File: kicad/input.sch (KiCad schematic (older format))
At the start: 4 parts, among them J2 EXTERNAL_OUT, J3 EXTERNAL_IN

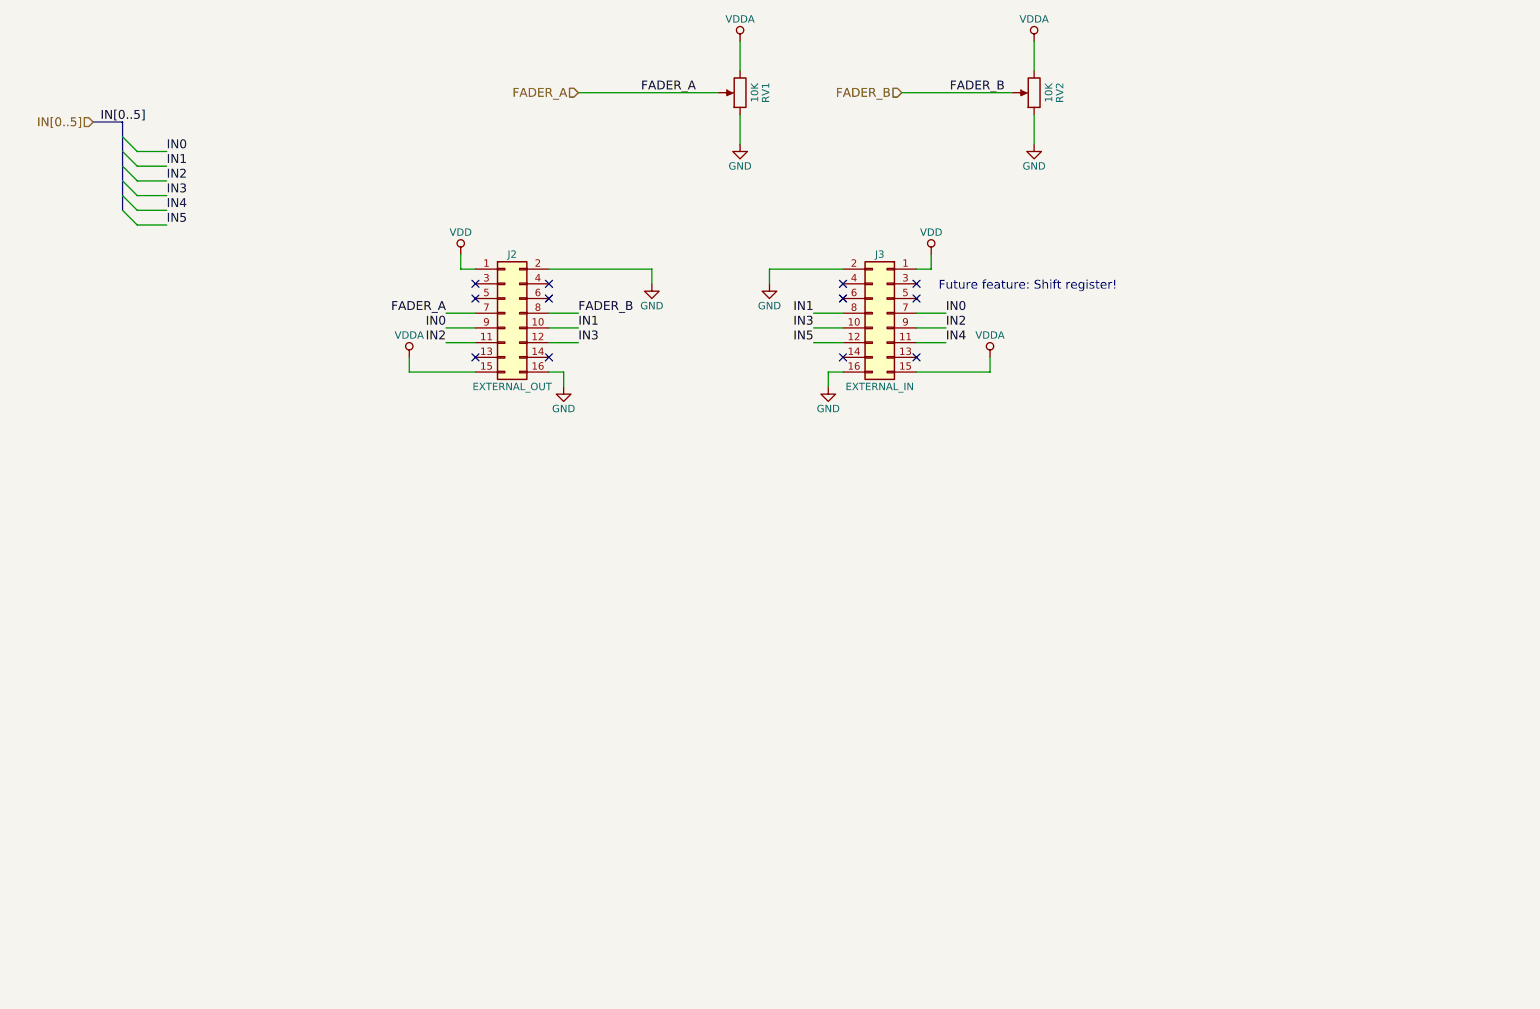
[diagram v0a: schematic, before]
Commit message: Created shift register circuitry and imported footprints
I think 5MHz to 10MHz is the theoretical maximum of this circuit. Actual
frequency will probably be around 5MHz or somewhat less given the signal
integrity issues on a 2-layer board with this many plane breaks.

Created footprints for button and HTSSOP

The HTSSOP footprint is special because I plan to hand solder, so I
added excessive thermal vias and a bare pad on the backside.

The netlist is imported to the PCB, but only the switches are placed.
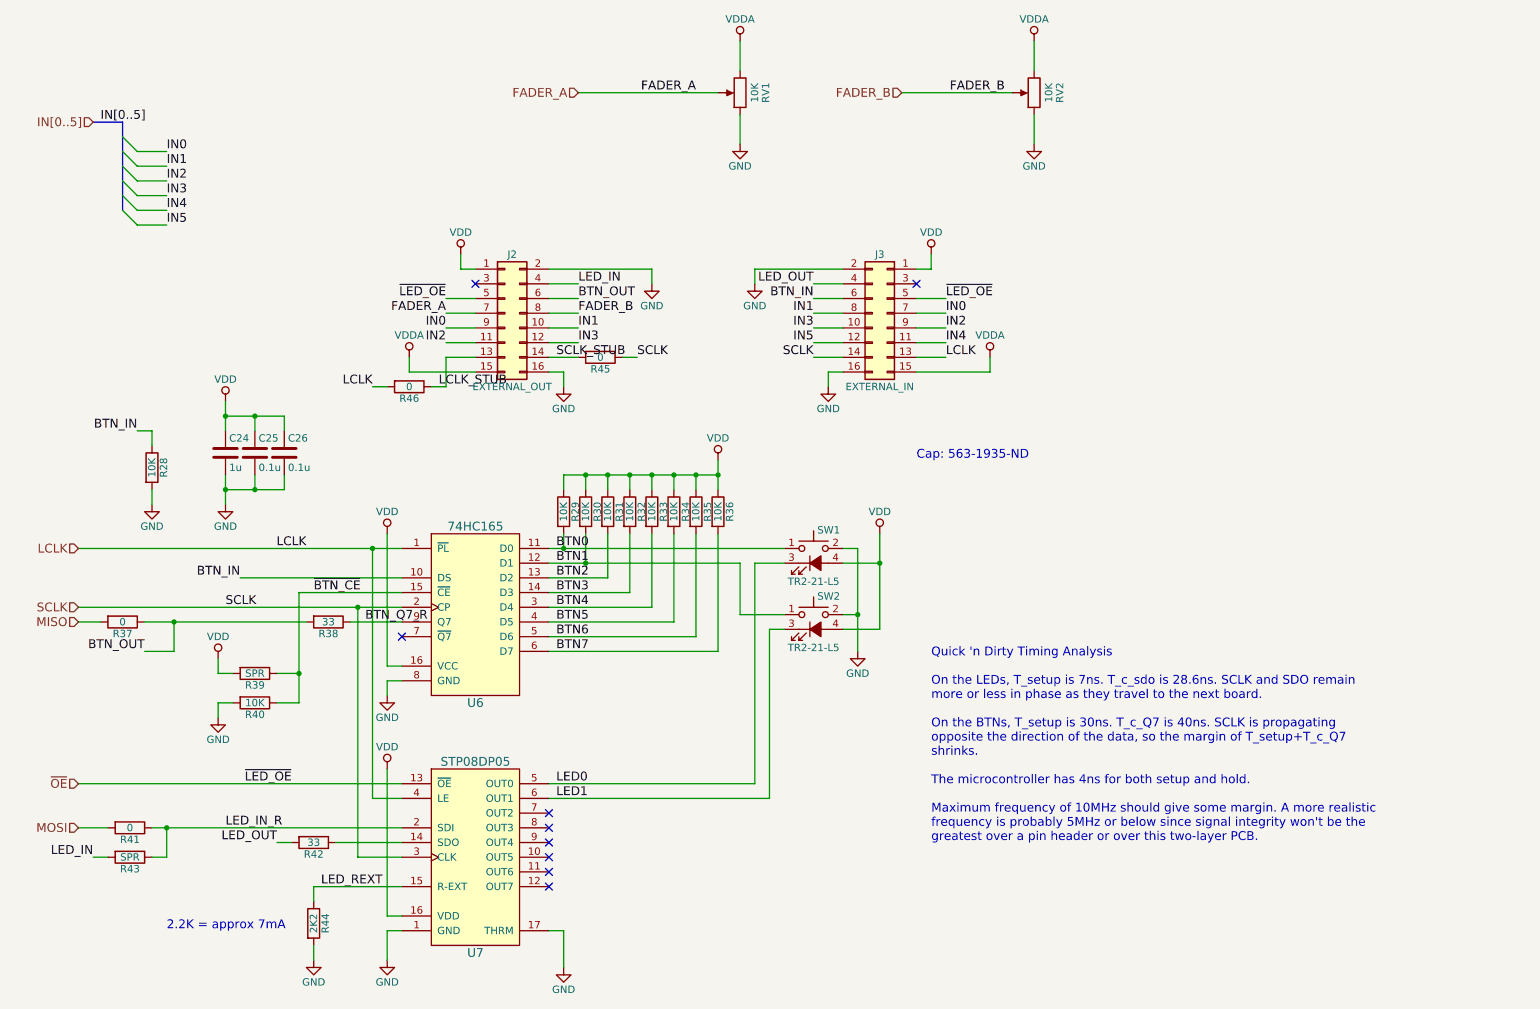
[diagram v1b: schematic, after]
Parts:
- added C24: 1u, Capacitors_SMD:C_0603, symbol C
- added C25, C26: 0.1u, Capacitors_SMD:C_0402, symbol C
- added R28, R29, R30, R31, R32, R33, R34, R35, R36, R40: 10K, Resistors_SMD:R_0402, symbol R
- added R37, R41, R45, R46: 0, Resistors_SMD:R_0402, symbol R
- added R38, R42: 33, Resistors_SMD:R_0402, symbol R
- added R39, R43: SPR, Resistors_SMD:R_0402, symbol R
- added R44: 2K2, Resistors_SMD:R_0402, symbol R
- added SW1, SW2: TR2-21-L5, midi-fader:Nidec_Copal_TR2, symbol SW_Push_LED
- added U6: 74HC165, Housings_SSOP:TSSOP-16_4.4x5mm_Pitch0.65mm, symbol 74HC165
- added U7: STP08DP05, midi-fader:HTSSOP-16-1EP_4.4x5mm_Pitch0.65mm_ThermalVias_HandSolder, symbol STP08DP05
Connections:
- net GND: now also C24.2, C25.2, C26.2, R28.2, R40.2, R44.2, SW1.2, SW2.2, U6.8 (GND), U7.1 (GND), U7.17 (THRM)
- net VDD: now also C24.1, C25.1, C26.1, R29.1, R30.1, R31.1, R32.1, R33.1, R34.1, R35.1, R36.1, R39.2, SW1.4 (A), SW2.4 (A), U6.16 (VCC), U7.16 (VDD)
- net LCLK_STUB: now reaches J2.13 (Pin_13)
- net LCLK_STUB: now also R46.1
- net SCLK_STUB: now reaches J2.14 (Pin_14)
- net SCLK_STUB: now also R45.2
- net LED_IN: now reaches J2.4 (Pin_4)
- net LED_IN: now also R43.2
- net ~OE: now reaches J2.5 (Pin_5)
- net ~OE: now also J3.5 (Pin_5), U7.13 (~OE)
- net BTN_OUT: now reaches J2.6 (Pin_6)
- net BTN_OUT: now also R37.1, R38.2
- net LCLK: now reaches J3.13 (Pin_13)
- net LCLK: now also R46.2, U6.1 (~PL), U7.4 (LE)
- net SCLK: now reaches J3.14 (Pin_14)
- net SCLK: now also R45.1, U6.2 (CP), U7.3 (CLK)
- net LED_OUT: now reaches J3.4 (Pin_4)
- net LED_OUT: now also R42.2
- net BTN_IN: now reaches J3.6 (Pin_6)
- net BTN_IN: now also R28.1, U6.10 (DS)
- new net: R42.1, U7.14 (SDO)
- new net BTN0: R29.2, SW1.1, U6.11 (D0)
- new net BTN1: R30.2, SW2.1, U6.12 (D1)
- new net BTN2: R31.2, U6.13 (D2)
- new net BTN3: R32.2, U6.14 (D3)
- new net BTN4: R33.2, U6.3 (D4)
- new net BTN5: R34.2, U6.4 (D5)
- new net BTN6: R35.2, U6.5 (D6)
- new net BTN7: R36.2, U6.6 (D7)
- new net BTN_Q7_R: R38.1, U6.9 (Q7)
- new net LED0: SW1.3 (K), U7.5 (OUT0)
- new net LED1: SW2.3 (K), U7.6 (OUT1)
- new net LED_IN_R: R41.1, R43.1, U7.2 (SDI)
- new net LED_REXT: R44.1, U7.15 (R-EXT)
- new net MISO: R37.2
- new net MOSI: R41.2
- new net ~BTN_CE: R39.1, R40.1, U6.15 (~CE)
- no-connect marks 12 -> 9
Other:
- note added: "2.2K = approx 7mA"
- note added: "Cap: 563-1935-ND"
- note added: "Quick 'n Dirty Timing Analysis\n\nOn the LEDs, T_setup is 7ns. T_c_sdo is 28.6ns. SCLK and SDO remain\nmore or less in phase as they travel to the next board.\n\nOn the BTNs, T_setup is 30ns. T_c_Q7 is 40ns. SCLK is propagating\nopposite the direction of the data, so the margin of T_setup+T_c_Q7\nshrinks.\n\nThe microcontroller has 4ns for both setup and hold.\n\nMaximum frequency of 10MHz should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"
- note removed: "Future feature: Shift register!"

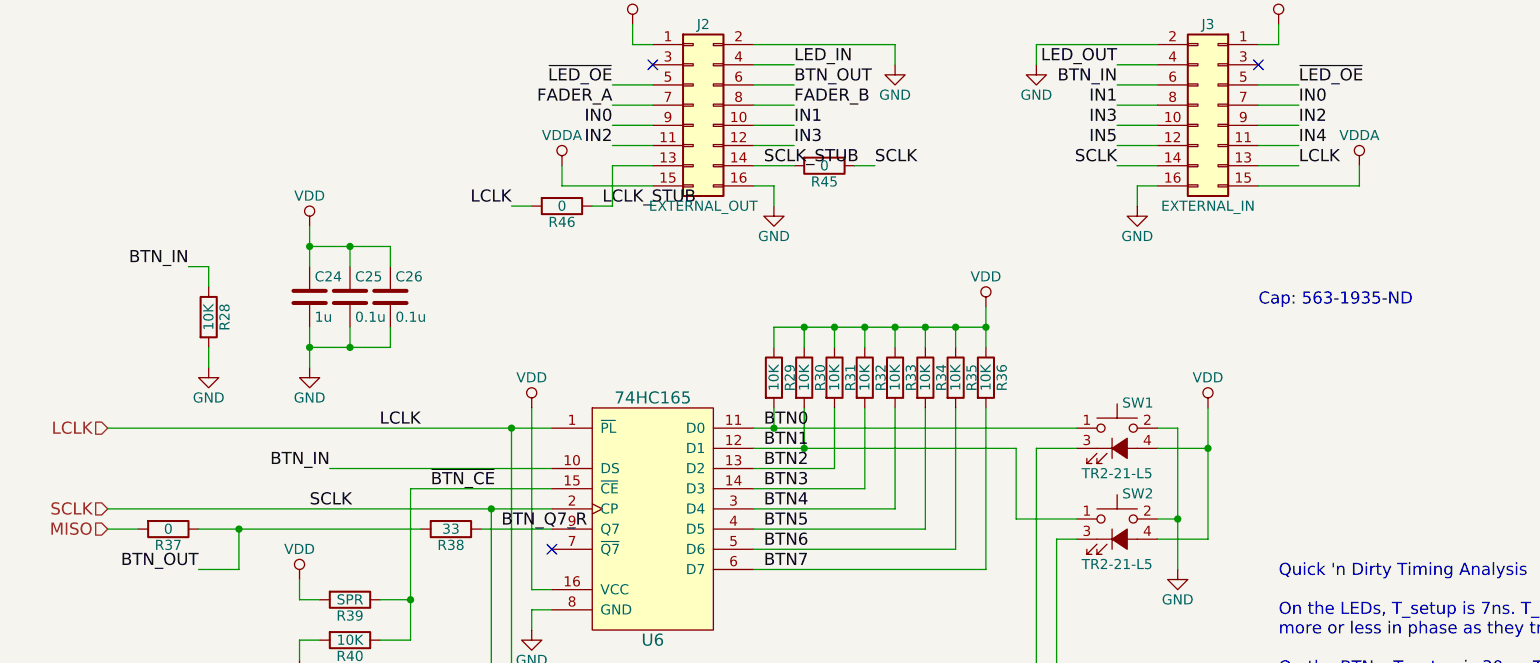
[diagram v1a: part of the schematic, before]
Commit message: Added stub-removal resistors on clock lines, started cleaning silkscreen
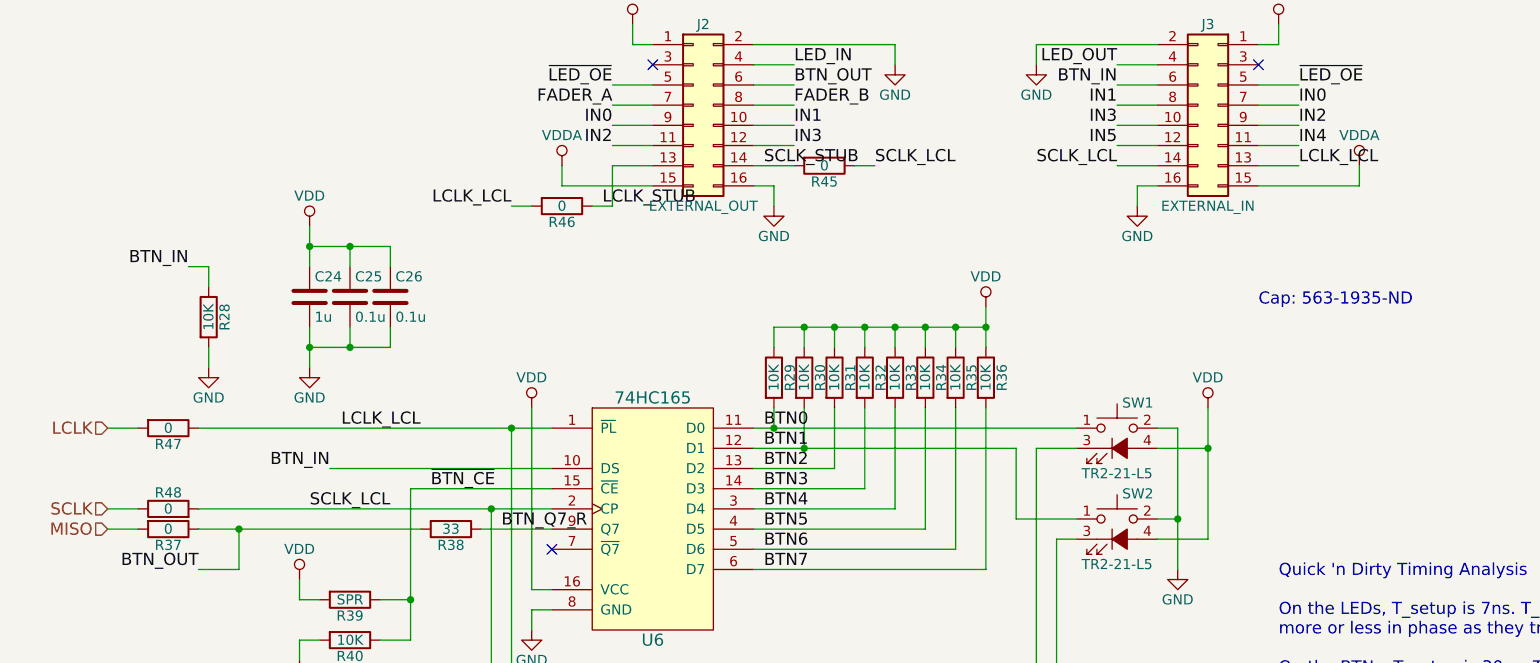
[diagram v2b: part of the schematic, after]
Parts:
- added R47, R48: 0, Resistors_SMD:R_0402, symbol R
- C24: Part No. (none) -> 1276-1182-1-ND
- C26: Part No. (none) -> 1276-1043-1-ND
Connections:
- net LCLK: now also R47.2; no longer J3.13 (Pin_13), R46.2, U6.1 (~PL), U7.4 (LE)
- net SCLK: now also R48.1; no longer J3.14 (Pin_14), R45.1, U6.2 (CP), U7.3 (CLK)
- new net LCLK_LCL: J3.13 (Pin_13), R46.2, R47.1, U6.1 (~PL), U7.4 (LE)
- new net SCLK_LCL: J3.14 (Pin_14), R45.1, R48.2, U6.2 (CP), U7.3 (CLK)
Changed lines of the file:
@@
 LED_REXT
 Text Label 2750 4400 2    60   ~ 0
-LCLK
+LCLK_LCL
 Text Label 2650 6000 2    60   ~ 0
 ~LED_OE
@@
 	2800 6700 2800 6800
 Wire Wire Line
-	1200 4400 3400 4400
-Wire Wire Line
 	3400 6100 3200 6100
 Wire Wire Line
@@
 Wire Wire Line
 	1200 6000 3400 6000
-Wire Wire Line
-	1200 4800 3400 4800
 Wire Wire Line
 	3400 6500 3100 6500
@@
 Connection ~ 3100 4800
 Text Label 2200 4800 0    60   ~ 0
-SCLK
+SCLK_LCL
 $Comp
 L R R40
@@
 F 2 "Capacitors_SMD:C_0402" H 2638 3600 50  0001 C CNN
 F 3 "" H 2600 3750 50  0001 C CNN
+F 4 "1276-1043-1-ND" H 2600 3750 60  0001 C CNN "Part No."
 	1    2600 3750
 	1    0    0    -1
@@
 F 2 "Capacitors_SMD:C_0603" H 2238 3600 50  0001 C CNN
 F 3 "" H 2200 3750 50  0001 C CNN
+F 4 "1276-1182-1-ND" H 2200 3750 60  0001 C CNN "Part No."
 	1    2200 3750
 	1    0    0    -1
@@
 Connection ~ 2400 4000
 Text Label 5000 3100 0    60   ~ 0
-SCLK
+SCLK_LCL
 Wire Wire Line
 	4600 3100 4400 3100
 Text Label 6200 3100 2    60   ~ 0
-SCLK
+SCLK_LCL
 Wire Wire Line
 	6200 3100 6400 3100
 Text Label 3200 3300 2    60   ~ 0
-LCLK
+LCLK_LCL
 Wire Wire Line
 	3700 3100 3900 3100
 Text Label 7100 3100 0    60   ~ 0
-LCLK
+LCLK_LCL
 Wire Wire Line
 	6900 3100 7100 3100
@@
 Wire Wire Line
 	7100 2700 6900 2700
+$Comp
+L R R48
+U 1 1 5B494DB5
+P 1500 4800
+F 0 "R48" V 1580 4800 50  0000 C CNN
+F 1 "0" V 1500 4800 50  0000 C CNN
+F 2 "Resistors_SMD:R_0402" V 1430 4800 50  0001 C CNN
+F 3 "" H 1500 4800 50  0001 C CNN
+	1    1500 4800
+	0    -1   -1   0
+$EndComp
+$Comp
+L R R47
+U 1 1 5B494F5F
+P 1500 4400
+F 0 "R47" V 1580 4400 50  0000 C CNN
+F 1 "0" V 1500 4400 50  0000 C CNN
+F 2 "Resistors_SMD:R_0402" V 1430 4400 50  0001 C CNN
+F 3 "" H 1500 4400 50  0001 C CNN
+	1    1500 4400
+	0    1    1    0
+$EndComp
+Wire Wire Line
+	1200 4400 1350 4400
+Wire Wire Line
+	1200 4800 1350 4800
+Wire Wire Line
+	1650 4400 3400 4400
+Wire Wire Line
+	1650 4800 3400 4800
 $EndSCHEMATC
